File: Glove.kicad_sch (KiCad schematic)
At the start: 53 parts, among them J1 USB_C_Receptacle_USB2.0_14P, J2 Conn_01x08, J3 Conn_01x02_Socket, SW2 SW_SPDT, SW3 TS-1187A-B-A-B, U1 ESP32-C3-WROOM-02, U2 XC6220B331MR, U3 PCA9546APW,118, U5 DRV2605YZFR, U6 DRV2605YZFR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

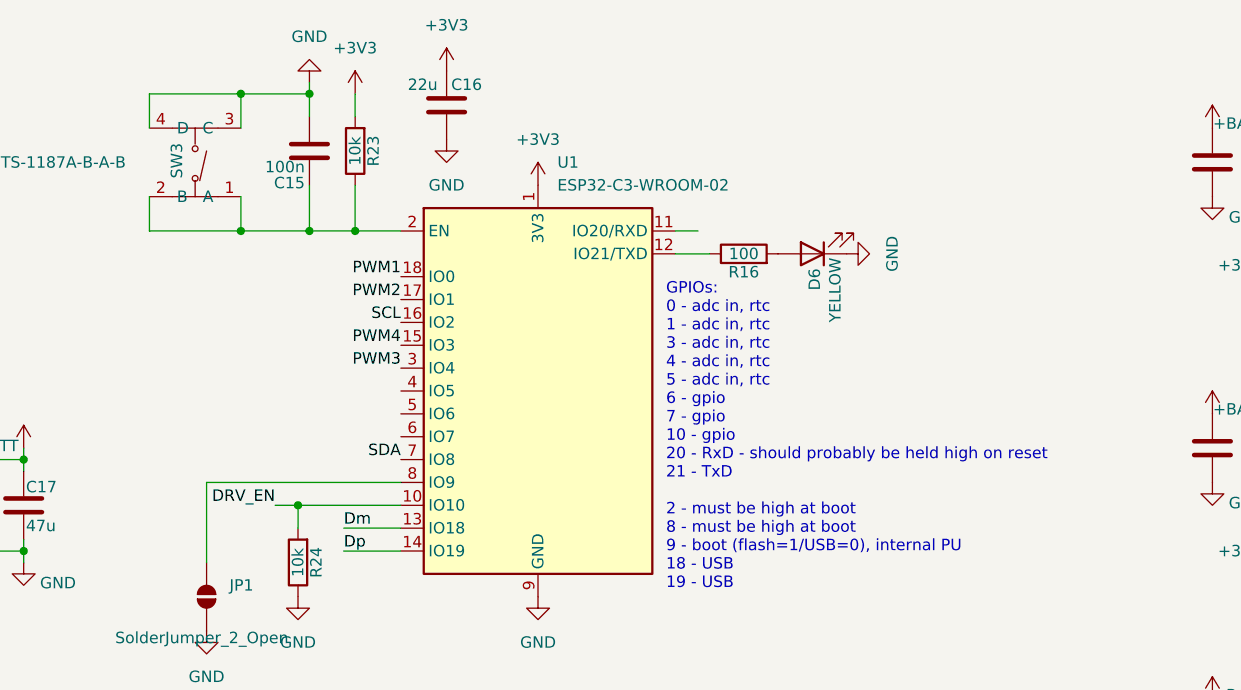
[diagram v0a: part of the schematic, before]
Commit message: Added button connector
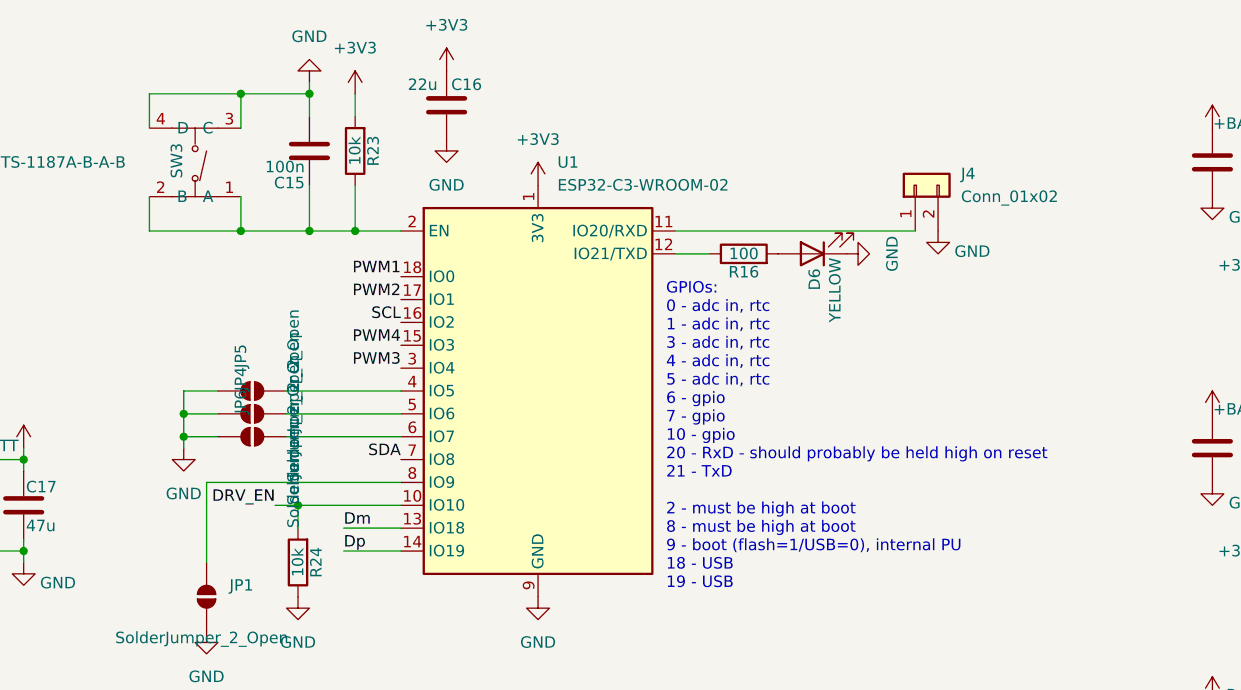
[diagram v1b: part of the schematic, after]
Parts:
- added J4: Conn_01x02, Connector_PinHeader_2.54mm:PinHeader_1x02_P2.54mm_Vertical, symbol Connector_Generic:Conn_01x02
- added JP4, JP5, JP6: SolderJumper_2_Open, Jumper:SolderJumper-2_P1.3mm_Open_RoundedPad1.0x1.5mm, symbol Jumper:SolderJumper_2_Open
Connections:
- net GND: now also J4.2 (Pin_2), JP4.2 (B), JP5.2 (B), JP6.2 (B)
- net at U1.11 (IO20/RXD): now also J4.1 (Pin_1)
- net at U1.4 (IO5): now also JP5.1 (A)
- net at U1.5 (IO6): now also JP4.1 (A)
- net at U1.6 (IO7): now also JP6.1 (A)
